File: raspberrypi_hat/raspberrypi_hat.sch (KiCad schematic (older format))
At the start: 18 parts, among them J3 40HAT, J6 CONN_02X02, J9 CONN_01X02, Q1 DMG2305UX, Q2 DMMT5401, U2 CAT24C32

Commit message: Update raspberrypi hat for new lib
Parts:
- H1, H2, H3, H4: symbol 3mm_Mounting_Hole -> Mechanical:Mounting_Hole
- J3: footprint Socket_Strips:Socket_Strip_Straight_2x20 -> Connector_PinSocket_2.54mm:PinSocket_2x20_P2.54mm_Vertical; symbol OX40HAT -> raspberrypi_hat:OX40HAT
- J6: footprint Pin_Headers:Pin_Header_Straight_2x02 -> Connector_PinHeader_2.54mm:PinHeader_2x02_P2.54mm_Vertical; symbol CONN_02X02 -> Connector_Generic:Conn_02x02_Odd_Even
- J9: footprint Pin_Headers:Pin_Header_Straight_1x02 -> Connector_PinHeader_2.54mm:PinHeader_1x02_P2.54mm_Vertical; symbol CONN_01X02 -> Connector_Generic:Conn_01x02
- Q1: footprint TO_SOT_Packages_SMD:SOT-23 -> Package_TO_SOT_SMD:SOT-23; symbol DMG2305UX -> raspberrypi_hat:DMG2305UX
- Q2: footprint TO_SOT_Packages_SMD:SOT-23-6 -> Package_TO_SOT_SMD:SOT-23-6; symbol DMMT5401 -> raspberrypi_hat:DMMT5401
- R11, R7, R9: footprint Resistors_SMD:R_0805_HandSoldering -> Resistor_SMD:R_0603_1608Metric_Pad0.84x1.00mm_HandSolder; symbol R -> Device:R
- R23, R24, R29, R6, R8: footprint Resistors_SMD:R_0603_HandSoldering -> Resistor_SMD:R_0603_1608Metric_Pad0.84x1.00mm_HandSolder; symbol R -> Device:R
- U2: footprint Housings_SOIC:SOIC-8_3.9x4.9mm_Pitch1.27mm -> Package_SOIC:SOIC-8_3.9x4.9mm_P1.27mm; symbol CAT24C32 -> raspberrypi_hat:CAT24C32
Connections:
- wire segments 65 -> 82

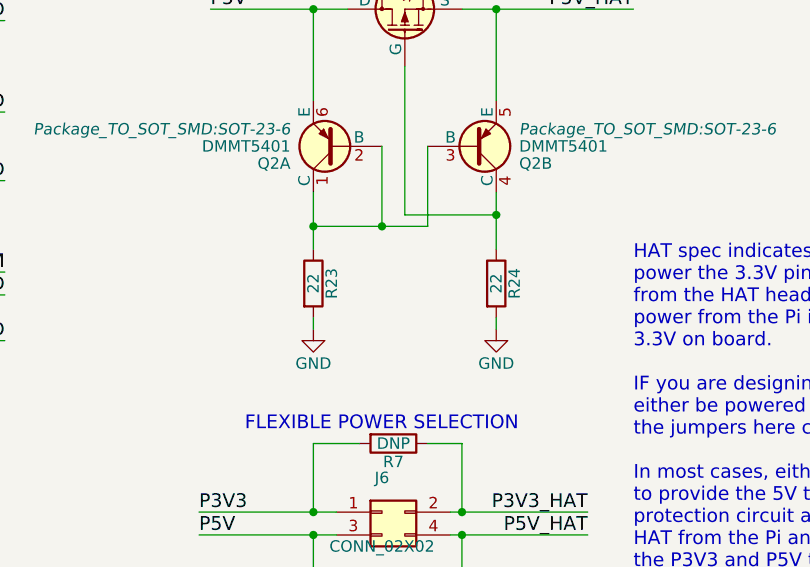
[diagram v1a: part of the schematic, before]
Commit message: Fix value on ideal diode collector resistors
Also remove excessive properties on resistors and mounting holes.
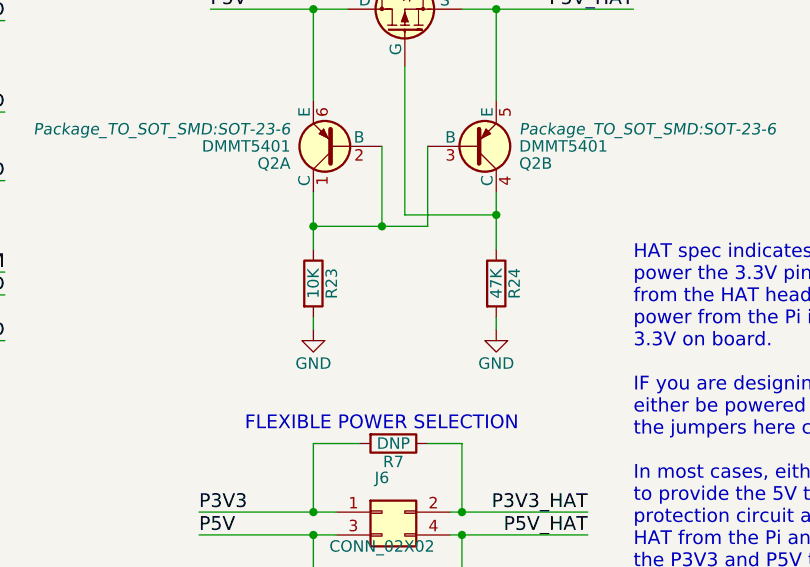
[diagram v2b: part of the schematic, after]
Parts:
- R11, R29, R6, R7, R8, R9: MFR Yageo -> (none); MPN RC0402JR-0722RL -> (none); SPN 311-22JRCT-ND -> (none); SPR Digikey -> (none)
- R23: value 22 -> 10K; MFR Yageo -> (none); MPN RC0402JR-0722RL -> (none); SPN 311-22JRCT-ND -> (none); SPR Digikey -> (none)
- R24: value 22 -> 47K; MFR Yageo -> (none); MPN RC0402JR-0722RL -> (none); SPN 311-22JRCT-ND -> (none); SPR Digikey -> (none)
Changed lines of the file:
@@
 F 2 "project_footprints:NPTH_3mm_ID" H 5550 6000 60  0001 C CNN
 F 3 "" H 5550 6000 60  0001 C CNN
-F 4 "" H -12600 -4650 50  0001 C CNN "MFR"
-F 5 "" H -12600 -4650 50  0001 C CNN "MPN"
-F 6 "" H -12600 -4650 50  0001 C CNN "SPR"
-F 7 "" H -12600 -4650 50  0001 C CNN "SPN"
-F 8 "" H -12600 -4650 50  0001 C CNN "SPURL"
 	1    5650 6000
 	1    0    0    -1
@@
 F 2 "project_footprints:NPTH_3mm_ID" H 6550 6000 60  0001 C CNN
 F 3 "" H 6550 6000 60  0001 C CNN
-F 4 "" H -12600 -4650 50  0001 C CNN "MFR"
-F 5 "" H -12600 -4650 50  0001 C CNN "MPN"
-F 6 "" H -12600 -4650 50  0001 C CNN "SPR"
-F 7 "" H -12600 -4650 50  0001 C CNN "SPN"
-F 8 "" H -12600 -4650 50  0001 C CNN "SPURL"
 	1    6650 6000
 	1    0    0    -1
@@
 F 2 "project_footprints:NPTH_3mm_ID" H 5550 6550 60  0001 C CNN
 F 3 "" H 5550 6550 60  0001 C CNN
-F 4 "" H -12600 -4650 50  0001 C CNN "MFR"
-F 5 "" H -12600 -4650 50  0001 C CNN "MPN"
-F 6 "" H -12600 -4650 50  0001 C CNN "SPR"
-F 7 "" H -12600 -4650 50  0001 C CNN "SPN"
-F 8 "" H -12600 -4650 50  0001 C CNN "SPURL"
 	1    5650 6550
 	1    0    0    -1
@@
 F 2 "project_footprints:NPTH_3mm_ID" H 6600 6550 60  0001 C CNN
 F 3 "" H 6600 6550 60  0001 C CNN
-F 4 "" H -12600 -4650 50  0001 C CNN "MFR"
-F 5 "" H -12600 -4650 50  0001 C CNN "MPN"
-F 6 "" H -12600 -4650 50  0001 C CNN "SPR"
-F 7 "" H -12600 -4650 50  0001 C CNN "SPN"
-F 8 "" H -12600 -4650 50  0001 C CNN "SPURL"
 	1    6700 6550
 	1    0    0    -1
@@
 P 5750 3600
 F 0 "R23" V 5830 3600 50  0000 C CNN
-F 1 "22" V 5750 3600 50  0000 C CNN
+F 1 "10K" V 5750 3600 50  0000 C CNN
 F 2 "Resistor_SMD:R_0603_1608Metric_Pad0.84x1.00mm_HandSolder" V 5680 3600 50  0001 C CNN
 F 3 "" H 5750 3600 50  0001 C CNN
-F 4 "Yageo" H -9800 -10750 50  0001 C CNN "MFR"
-F 5 "RC0402JR-0722RL" H -9800 -10750 50  0001 C CNN "MPN"
-F 6 "Digikey" H -9800 -10750 50  0001 C CNN "SPR"
-F 7 "311-22JRCT-ND" H -9800 -10750 50  0001 C CNN "SPN"
-F 8 "" H -9800 -10750 50  0001 C CNN "SPURL"
 	1    5750 3600
 	1    0    0    -1
@@
 P 6550 3600
 F 0 "R24" V 6630 3600 50  0000 C CNN
-F 1 "22" V 6550 3600 50  0000 C CNN
+F 1 "47K" V 6550 3600 50  0000 C CNN
 F 2 "Resistor_SMD:R_0603_1608Metric_Pad0.84x1.00mm_HandSolder" V 6480 3600 50  0001 C CNN
 F 3 "" H 6550 3600 50  0001 C CNN
-F 4 "Yageo" H -9000 -10950 50  0001 C CNN "MFR"
-F 5 "RC0402JR-0722RL" H -9000 -10950 50  0001 C CNN "MPN"
-F 6 "Digikey" H -9000 -10950 50  0001 C CNN "SPR"
-F 7 "311-22JRCT-ND" H -9000 -10950 50  0001 C CNN "SPN"
-F 8 "" H -9000 -10950 50  0001 C CNN "SPURL"
 	1    6550 3600
 	1    0    0    -1
@@
 F 2 "Resistor_SMD:R_0603_1608Metric_Pad0.84x1.00mm_HandSolder" V 2280 7400 50  0001 C CNN
 F 3 "" H 2350 7400 50  0001 C CNN
-F 4 "Yageo" H -13200 -6950 50  0001 C CNN "MFR"
-F 5 "RC0402JR-0722RL" H -13200 -6950 50  0001 C CNN "MPN"
-F 6 "Digikey" H -13200 -6950 50  0001 C CNN "SPR"
-F 7 "311-22JRCT-ND" H -13200 -6950 50  0001 C CNN "SPN"
-F 8 "" H -13200 -6950 50  0001 C CNN "SPURL"
 	1    2350 7400
 	0    1    1    0
@@
 F 2 "Resistor_SMD:R_0603_1608Metric_Pad0.84x1.00mm_HandSolder" V 2280 7650 50  0001 C CNN
 F 3 "" H 2350 7650 50  0001 C CNN
-F 4 "Yageo" H -13200 -6700 50  0001 C CNN "MFR"
-F 5 "RC0402JR-0722RL" H -13200 -6700 50  0001 C CNN "MPN"
-F 6 "Digikey" H -13200 -6700 50  0001 C CNN "SPR"
-F 7 "311-22JRCT-ND" H -13200 -6700 50  0001 C CNN "SPN"
-F 8 "" H -13200 -6700 50  0001 C CNN "SPURL"
 	1    2350 7650
 	0    1    1    0
@@
 F 2 "Resistor_SMD:R_0603_1608Metric_Pad0.84x1.00mm_HandSolder" V 1480 6250 50  0001 C CNN
 F 3 "" H 1550 6250 50  0001 C CNN
-F 4 "Yageo" H -14000 -8100 50  0001 C CNN "MFR"
-F 5 "RC0402JR-0722RL" H -14000 -8100 50  0001 C CNN "MPN"
-F 6 "Digikey" H -14000 -8100 50  0001 C CNN "SPR"
-F 7 "311-22JRCT-ND" H -14000 -8100 50  0001 C CNN "SPN"
-F 8 "" H -14000 -8100 50  0001 C CNN "SPURL"
 	1    1550 6250
 	-1   0    0    1
@@
 F 2 "Resistor_SMD:R_0603_1608Metric_Pad0.84x1.00mm_HandSolder" V 6030 4300 50  0001 C CNN
 F 3 "" H 6100 4300 50  0001 C CNN
-F 4 "Yageo" H -9450 -10050 50  0001 C CNN "MFR"
-F 5 "RC0402JR-0722RL" H -9450 -10050 50  0001 C CNN "MPN"
-F 6 "Digikey" H -9450 -10050 50  0001 C CNN "SPR"
-F 7 "311-22JRCT-ND" H -9450 -10050 50  0001 C CNN "SPN"
-F 8 "" H -9450 -10050 50  0001 C CNN "SPURL"
 	1    6100 4300
 	0    1    1    0
@@
 F 2 "Resistor_SMD:R_0603_1608Metric_Pad0.84x1.00mm_HandSolder" V 6030 4950 50  0001 C CNN
 F 3 "" H 6100 4950 50  0001 C CNN
-F 4 "Yageo" H -9450 -9400 50  0001 C CNN "MFR"
-F 5 "RC0402JR-0722RL" H -9450 -9400 50  0001 C CNN "MPN"
-F 6 "Digikey" H -9450 -9400 50  0001 C CNN "SPR"
-F 7 "311-22JRCT-ND" H -9450 -9400 50  0001 C CNN "SPN"
-F 8 "" H -9450 -9400 50  0001 C CNN "SPURL"
 	1    6100 4950
 	0    1    1    0
@@
 F 2 "Resistor_SMD:R_0603_1608Metric_Pad0.84x1.00mm_HandSolder" V 1230 6100 50  0001 C CNN
 F 3 "" H 1300 6100 50  0001 C CNN
-F 4 "Yageo" H -14250 -8250 50  0001 C CNN "MFR"
-F 5 "RC0402JR-0722RL" H -14250 -8250 50  0001 C CNN "MPN"
-F 6 "Digikey" H -14250 -8250 50  0001 C CNN "SPR"
-F 7 "311-22JRCT-ND" H -14250 -8250 50  0001 C CNN "SPN"
-F 8 "" H -14250 -8250 50  0001 C CNN "SPURL"
 	1    1300 6100
 	0    1    1    0

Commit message: Fix incorrect SDA and SCL pin on Raspberry pi hat EEPROM
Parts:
- H1, H2, H3, H4: symbol Mechanical:Mounting_Hole -> Mechanical:MountingHole
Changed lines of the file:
@@
 EESchema Schematic File Version 4
 LIBS:raspberrypi_hat-cache
-EELAYER 26 0
+EELAYER 29 0
 EELAYER END
 $Descr A3 16535 11693
@@
 $EndDescr
 $Comp
-L Mechanical:Mounting_Hole H1
+L Mechanical:MountingHole H1
 U 1 1 5834BC4A
 P 5650 6000
@@
 $EndComp
 $Comp
-L Mechanical:Mounting_Hole H2
+L Mechanical:MountingHole H2
 U 1 1 5834BCDF
 P 6650 6000
@@
 $EndComp
 $Comp
-L Mechanical:Mounting_Hole H3
+L Mechanical:MountingHole H3
 U 1 1 5834BD62
 P 5650 6550
@@
 $EndComp
 $Comp
-L Mechanical:Mounting_Hole H4
+L Mechanical:MountingHole H4
 U 1 1 5834BDED
 P 6700 6550
@@
 Wire Wire Line
 	2600 5950 3450 5950
+Text Label 3450 6050 2    60   ~ 0
+ID_SD_EEPROM_pu
 Text Label 3450 5950 2    60   ~ 0
-ID_SD_EEPROM_pu
-Text Label 3450 6050 2    60   ~ 0
 ID_SC_EEPROM_pu
 $Comp
